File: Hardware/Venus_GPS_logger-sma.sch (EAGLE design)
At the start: 21 parts, among them U1 VENUS634SMD, U2 33nH, U3 V_REG_LDOSMD, U4 SPI_FLASH-X25XXSMD1

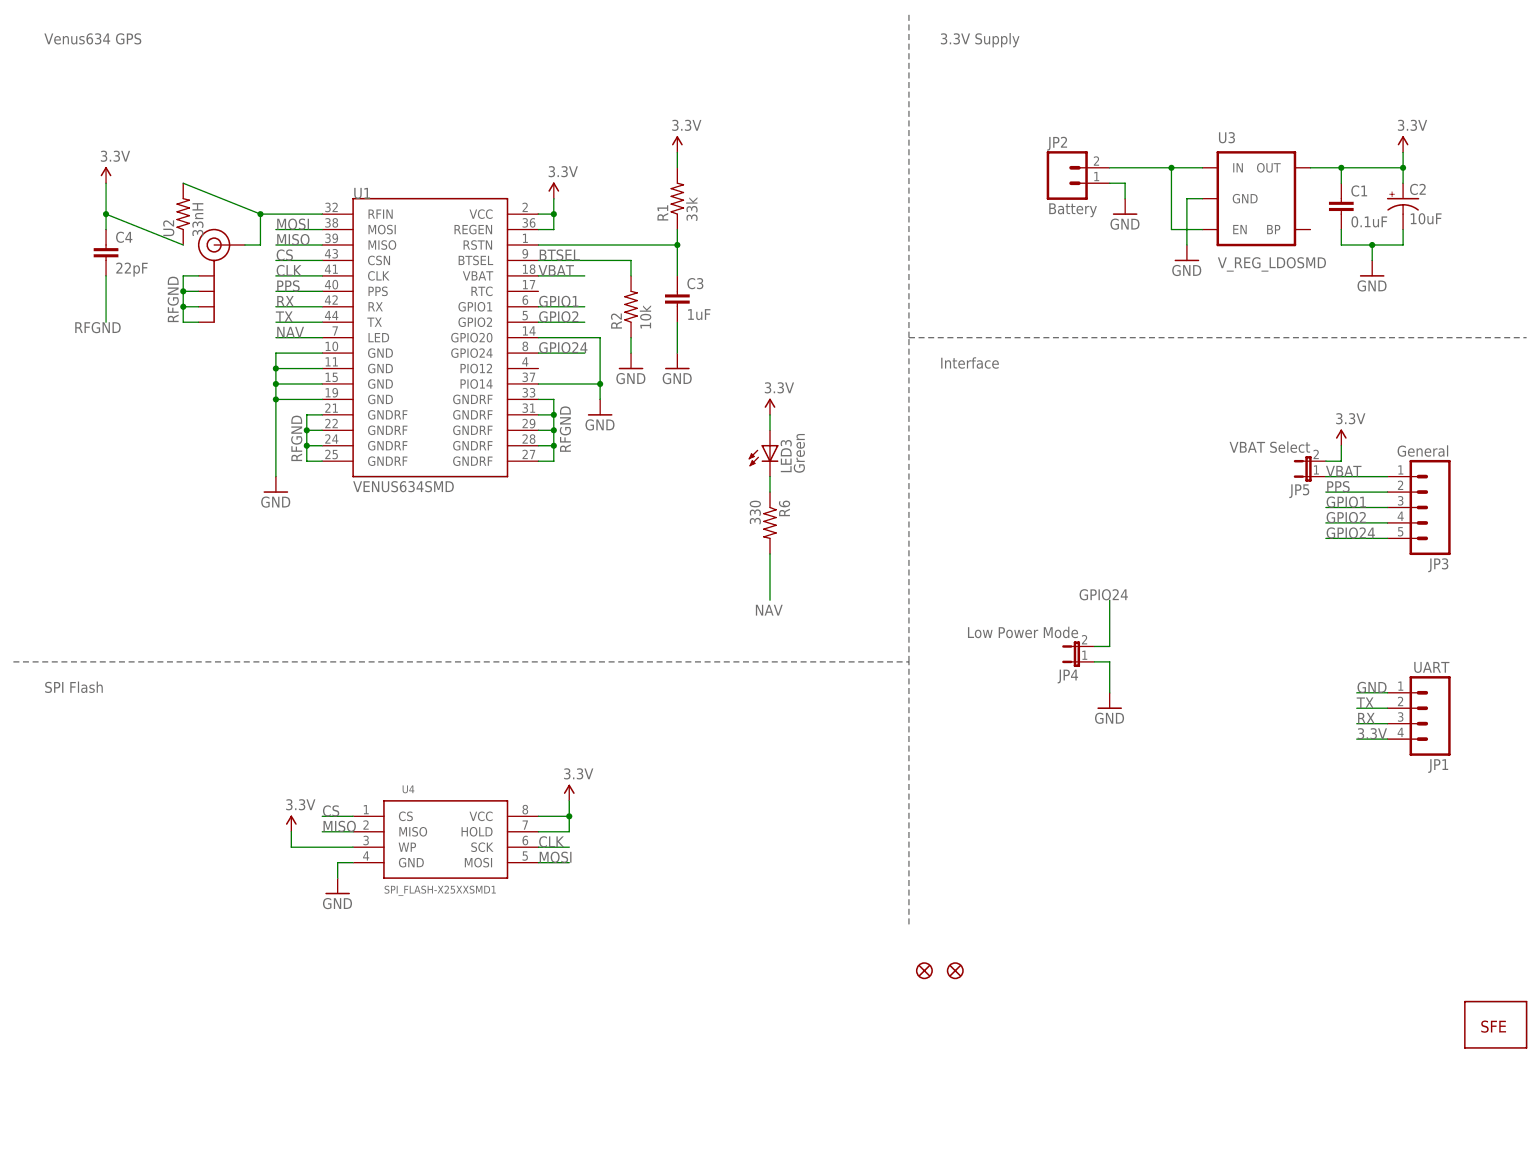
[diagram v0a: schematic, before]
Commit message: Updated LED, fixed questionable trace routes
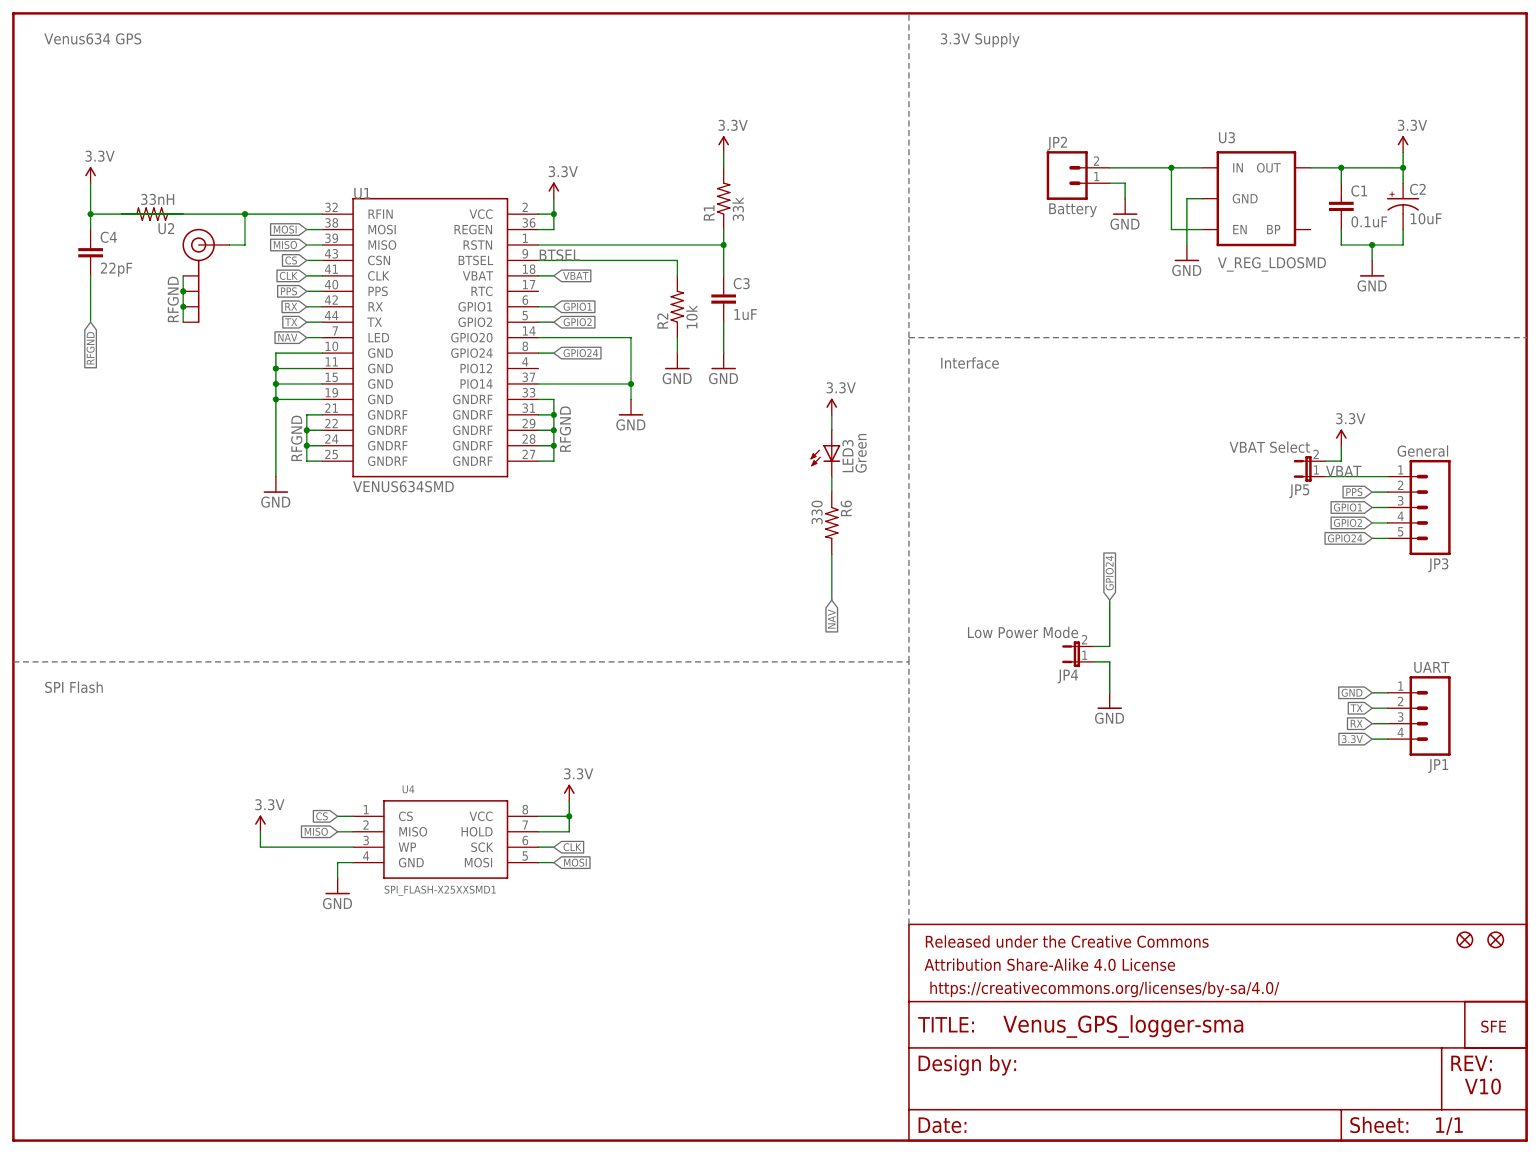
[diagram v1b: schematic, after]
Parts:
- added FRAME1: FRAME-LETTER, SparkFun-Aesthetics:FRAME-LETTER
- LED3: device SparkFun:LED0603 -> SparkFun-LED:LED-GREEN0603
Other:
- note added: "V10"
- moved on the sheet: C3, C4, LED3, R1, R2, R6, U2

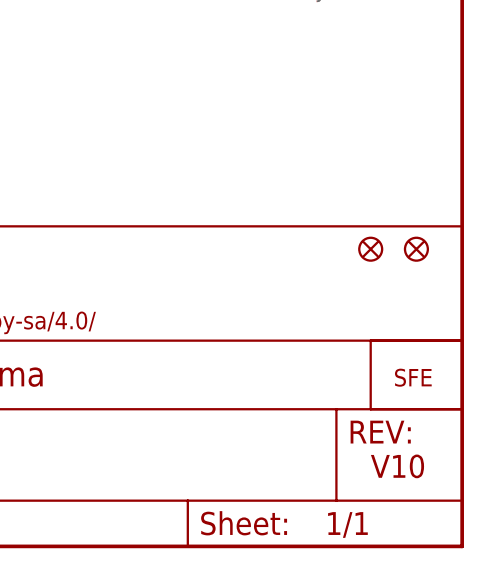
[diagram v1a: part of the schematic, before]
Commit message: changed fiducials to regular size and repositioned
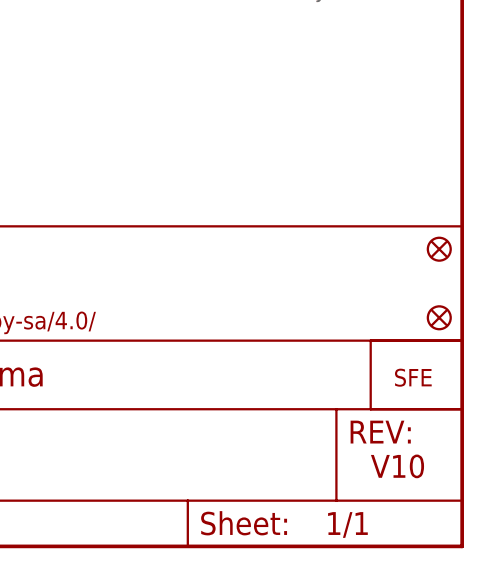
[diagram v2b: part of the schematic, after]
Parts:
- removed JP6, JP7: FIDUCIAL1X2.5, abes:FIDUCIAL1X2.5
- added FID1, FID2: FIDUCIAL1X2, SparkFun-Aesthetics:FIDUCIAL1X2
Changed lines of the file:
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@@
 <part name="JP4" library="SparkFun-Passives" deviceset="JUMPER-2" device="SMD-NC" value="Low Power Mode"/>
 <part name="JP5" library="SparkFun-Passives" deviceset="JUMPER-2" device="SMD-NC" value="VBAT Select"/>
-<part name="JP6" library="abes" deviceset="FIDUCIAL" device="1X2.5"/>
-<part name="JP7" library="abes" deviceset="FIDUCIAL" device="1X2.5"/>
+<part name="FID1" library="SparkFun-Aesthetics" deviceset="FIDUCIAL" device="1X2"/>
+<part name="FID2" library="SparkFun-Aesthetics" deviceset="FIDUCIAL" device="1X2"/>
 </parts>
 <sheets>
@@
 <instance part="JP4" gate="A" x="175.26" y="78.74" rot="R90"/>
 <instance part="JP5" gate="A" x="213.36" y="109.22" rot="R90"/>
-<instance part="JP6" gate="G$1" x="238.76" y="33.02"/>
-<instance part="JP7" gate="G$1" x="243.84" y="33.02"/>
+<instance part="FID1" gate="G$1" x="246.38" y="33.02"/>
+<instance part="FID2" gate="G$1" x="246.38" y="25.4"/>
 </instances>
 <busses>
